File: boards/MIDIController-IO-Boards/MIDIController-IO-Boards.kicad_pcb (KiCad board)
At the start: 2 copper layers, 150 x 100 mm, 51 parts, among them J1 KeyboardCtrl, J10 I2C, J11 LTC4311_1, J12 IO_Boards, J13 I2C2, J14 DC12V, J15 LTC4311_2, J2 TechnicsCtrl, J3 StopLeftCtrl, J4 StopRightCtrl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

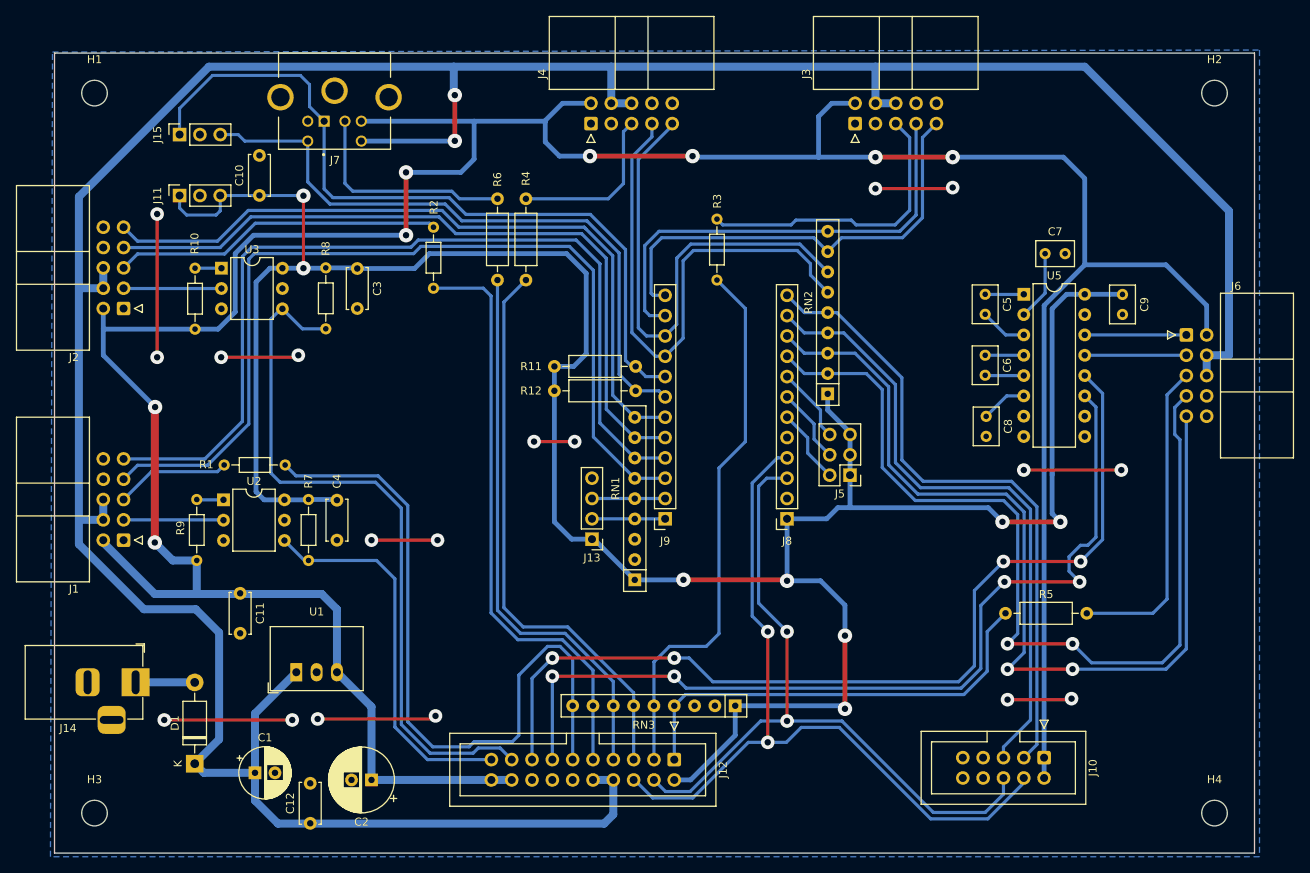
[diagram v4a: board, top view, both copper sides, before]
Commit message: Updated design rules to 0.32mm template and exported Gerber files
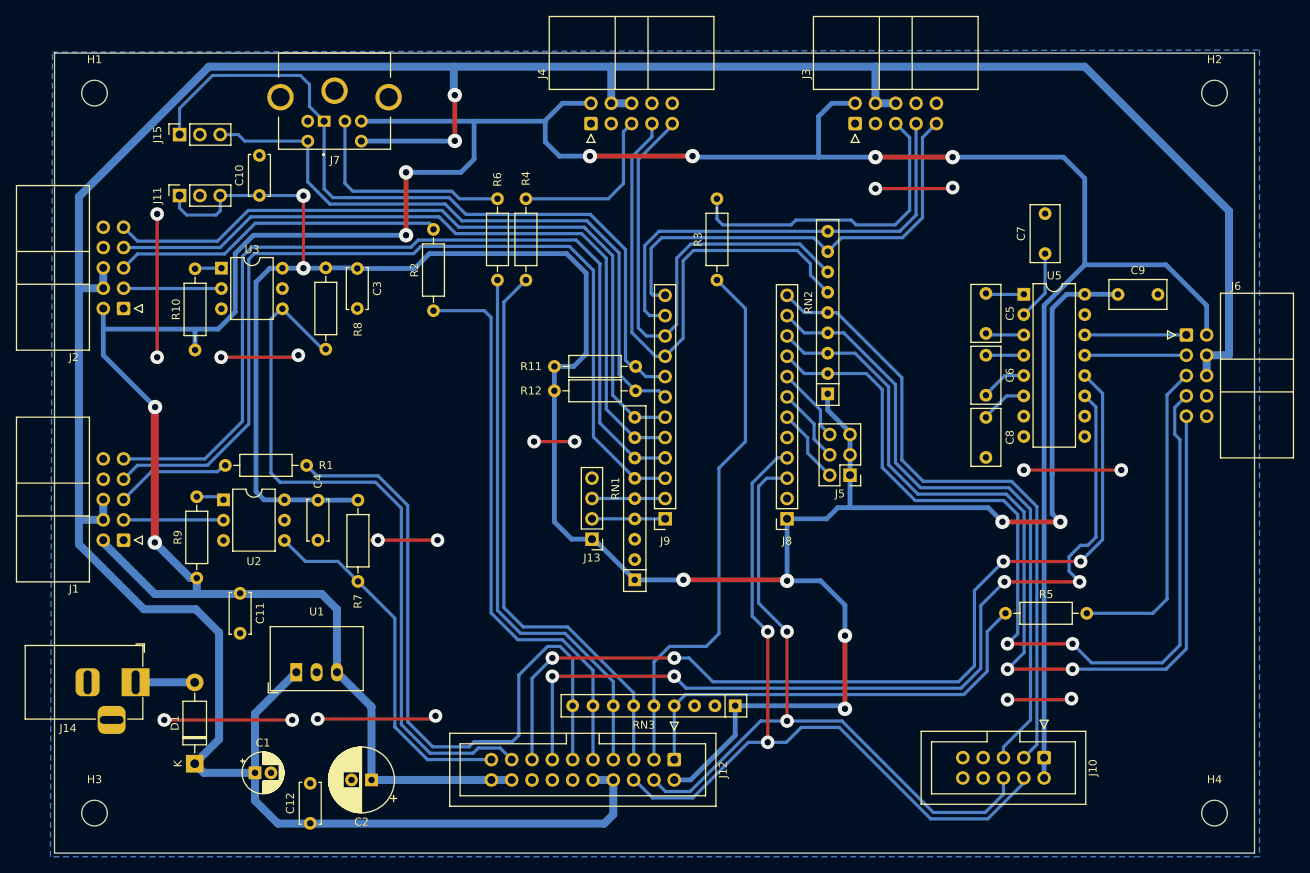
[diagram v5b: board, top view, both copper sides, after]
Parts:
- C1: footprint Capacitor_THT:CP_Radial_D6.3mm_P2.50mm -> Capacitor_THT:CP_Radial_D5.0mm_P2.00mm
- C5, C6, C7, C8, C9: footprint Capacitor_THT:C_Rect_L4.6mm_W3.0mm_P2.50mm_MKS02_FKP02 -> Capacitor_THT:C_Rect_L7.0mm_W3.5mm_P5.00mm
- R1, R10, R2, R3, R7, R8, R9: footprint Resistor_THT:R_Axial_DIN0204_L3.6mm_D1.6mm_P7.62mm_Horizontal -> Resistor_THT:R_Axial_DIN0207_L6.3mm_D2.5mm_P10.16mm_Horizontal
- moved R7 6.18 mm to (106.0, 96.3)
- moved R2 2.81 mm to (115.4, 72.7)
- moved R1 2.68 mm to (99.6, 92.0)
- moved R10 2.61 mm to (85.6, 77.6)
- moved C4 2.38 mm to (101.0, 96.3)
- moved R9 2.19 mm to (85.9, 106.1)
- moved C9 0.57 mm to (201.0, 70.6), turned to 0 degrees
- moved C5 0.15 mm to (184.5, 70.5)
- moved C8 0.13 mm to (184.5, 86.0)
- moved C6 0.10 mm to (184.5, 78.2)
- turned C7 to 90 degrees
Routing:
- net /RXD_Kbd: track 48.1 -> 45.2 mm
- net +3.3V: track 318.8 -> 321.6 mm
- net /IntTechnics: track 74.1 -> 71.4 mm
- net /IntKeyboard: track 89.2 -> 86.5 mm
- net Net-(J3-Pin_5): track 37.2 -> 39.7 mm
- net +5V: track 394.4 -> 395.8 mm
- net Net-(U5-C2-): track 4.70 -> 5.84 mm
- net /RXD_Technics: track 88.8 -> 89.9 mm
- net Net-(U5-C1-): track 5.89 -> 4.91 mm

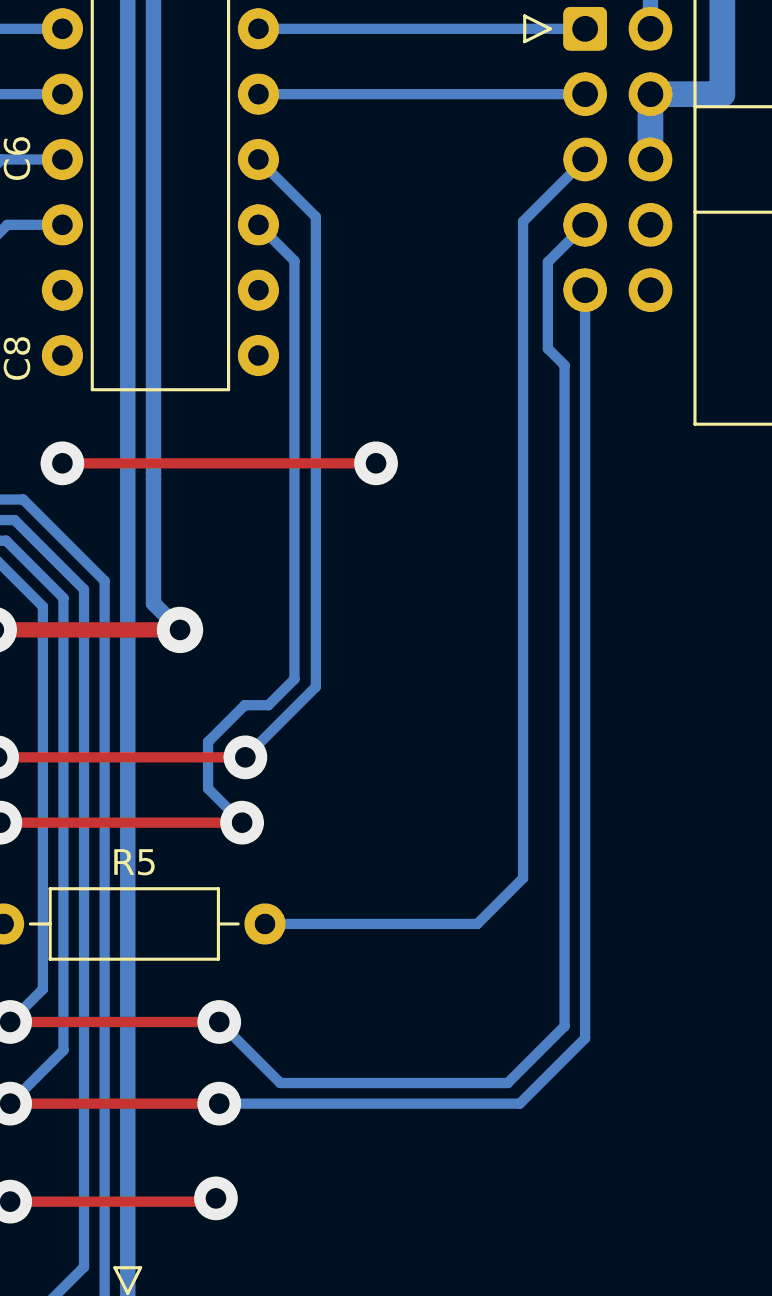
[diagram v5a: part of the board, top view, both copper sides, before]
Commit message: Fixed some RX/TX pin swaps
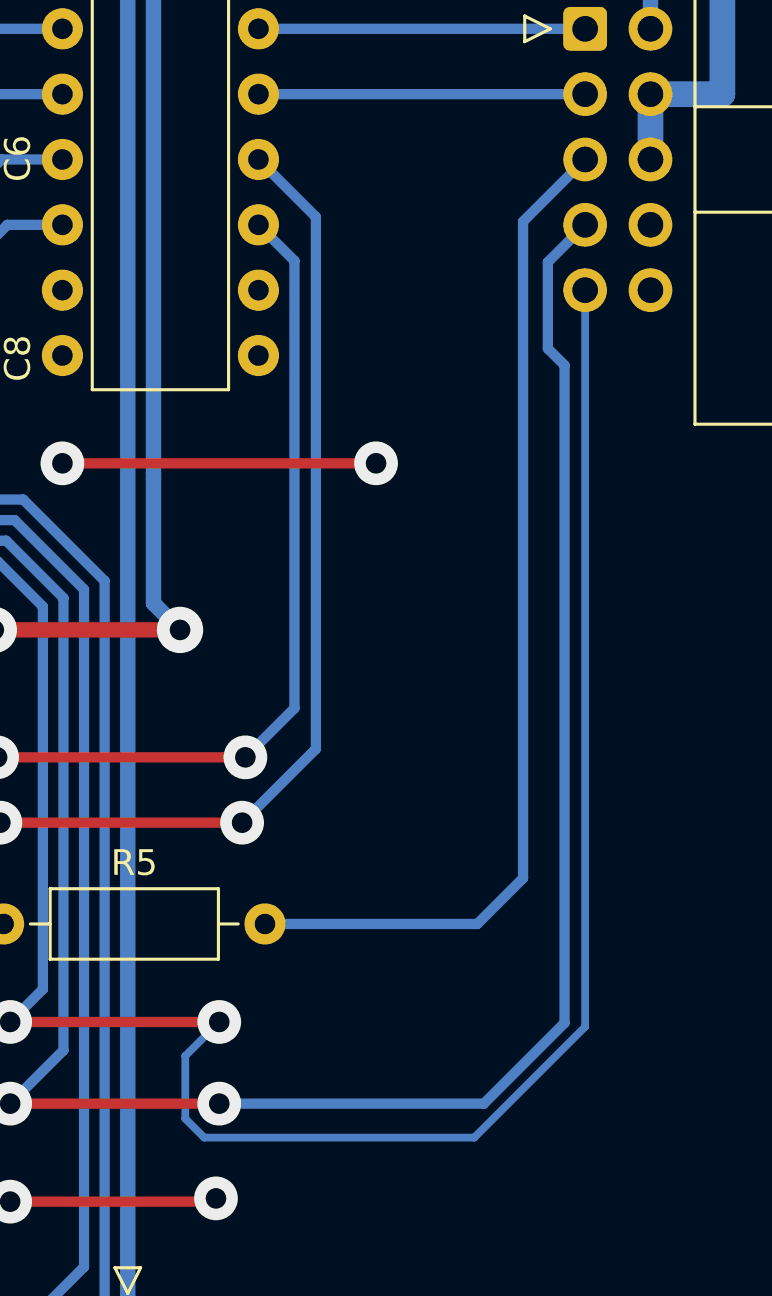
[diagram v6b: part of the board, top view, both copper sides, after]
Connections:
- J12 pad 13: /TXD_Panel -> /RXD_Panel
- J12 pad 15: /RXD_Panel -> /TXD_Panel
- J8 pad 10: /SDA_Panel -> /SCL_Panel
- J8 pad 9: /SCL_Panel -> /SDA_Panel
- RN2 pad 2: /SCL_Panel -> /SDA_Panel
- RN2 pad 3: /SDA_Panel -> /SCL_Panel
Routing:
- net /SCL_Panel: track 114.9 -> 119.7 mm
- net /RXD_Panel: track 117.8 -> 115.0 mm
- net /TXD_Panel: track 113.4 -> 114.6 mm
- net /SDA_Panel: track 117.5 -> 118.1 mm

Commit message: Fixed size of I2C expander board footprint
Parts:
- RN1, RN2: value 1.5k -> 1k
- RN3: value 1.5k -> 4k7
- moved J5 2.92 mm to (170.4, 93.2)
- moved J8 2.92 mm to (162.6, 98.7)
- moved RN2 2.92 mm to (167.6, 83.1)
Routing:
- net +3.3V: track 321.6 -> 318.1 mm
- net /SCL_StopRight: track 67.0 -> 69.9 mm
- net /SCL: track 98.7 -> 101.6 mm
- net /SDA_StopRight: track 62.2 -> 65.1 mm
- net /SDA_Panel: track 118.1 -> 115.2 mm
- net /SDA_I2C1: track 78.6 -> 75.7 mm
- net /SDA: track 90.4 -> 93.4 mm
- net /SCL_Panel: track 119.7 -> 116.8 mm
- net /SCL_I2C1: track 80.3 -> 77.3 mm
- net Net-(R9-Pad2): track 3.50 -> 2.96 mm

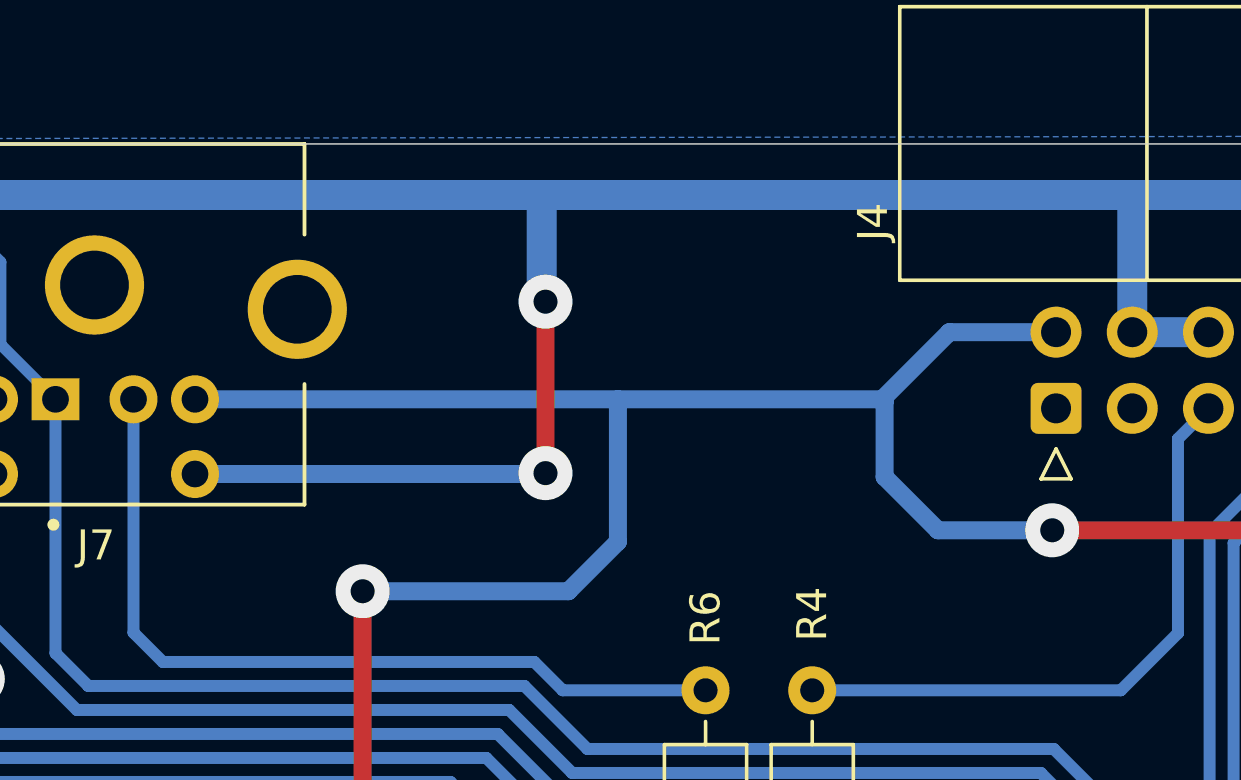
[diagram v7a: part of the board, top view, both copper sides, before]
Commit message: Make Toestud PS2 connectors symmetrical to avoid connection errors
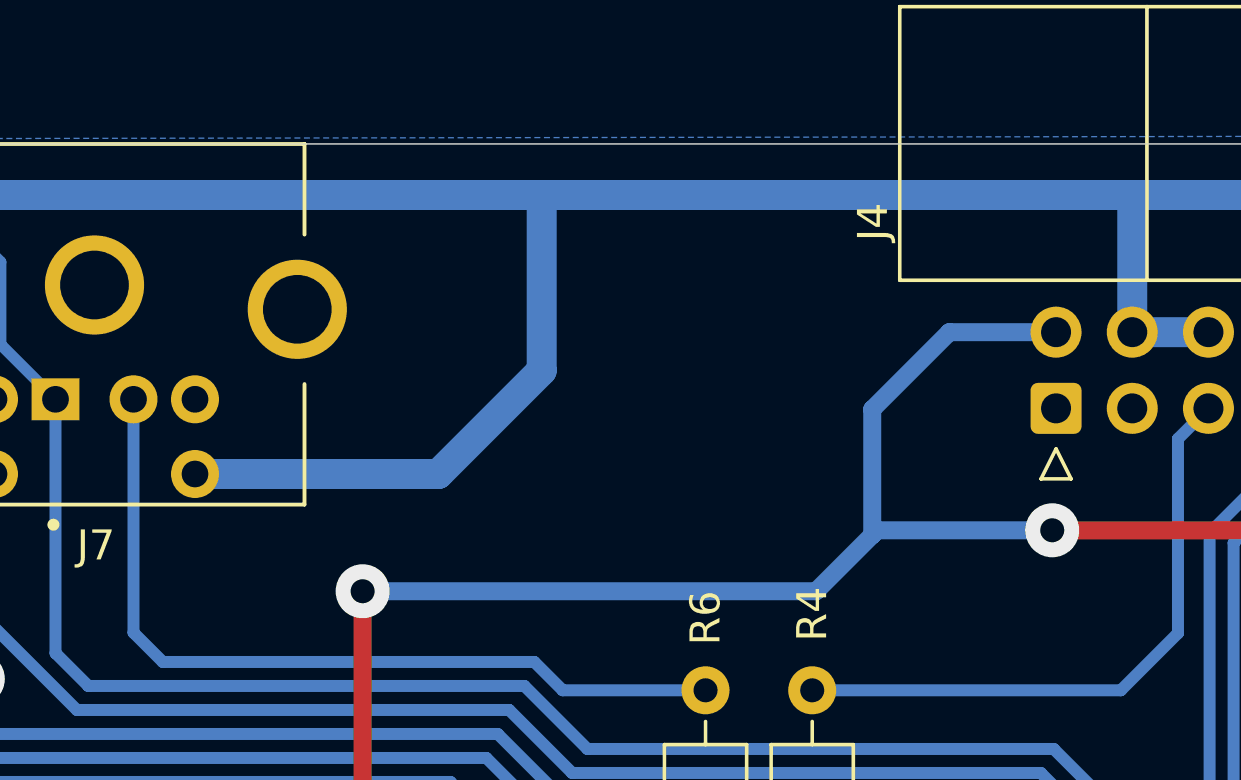
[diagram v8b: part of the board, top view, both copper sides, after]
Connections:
- J7 pad 4: +5V -> unconnected-(J7-Pad4)
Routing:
- net +5V: track 395.8 -> 378.5 mm
- net +12V: track 390.4 -> 388.3 mm, vias 2 -> 0
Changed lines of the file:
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@@
 	(net 69 "unconnected-(RN3-R2-Pad3)")
 	(net 70 "unconnected-(RN3-R1-Pad2)")
+	(net 71 "unconnected-(J7-Pad4)")
 	(footprint "Connector_IDC:IDC-Header_2x05_P2.54mm_Horizontal"
 		(layer "F.Cu")
@@
 			(layers "*.Cu" "*.Mask")
 			(remove_unused_layers no)
-			(net 4 "+5V")
-			(pintype "passive")
+			(net 71 "unconnected-(J7-Pad4)")
+			(pintype "passive+no_connect")
 			(solder_mask_margin 0.102)
 		)
@@
 	)
 	(segment
+		(start 131.572 46.736)
+		(end 135.128 46.736)
+		(width 0.6)
+		(layer "B.Cu")
+		(net 4)
+	)
+	(segment
 		(start 191.77 128.5335)
 		(end 191.77 131.0735)
@@
 	)
 	(segment
-		(start 135.001 53.34)
-		(end 131.191 53.34)
+		(start 127.128 55.372)
+		(end 129 53.5)
 		(width 0.6)
 		(layer "B.Cu")
@@
 	)
 	(segment
-		(start 129.413 49.053)
-		(end 129.334 48.974)
-		(width 0.6)
-		(layer "B.Cu")
-		(net 4)
-	)
-	(segment
 		(start 168.148 46.736)
 		(end 165.227 46.736)
@@
 	)
 	(segment
+		(start 129 49.308)
+		(end 131.572 46.736)
+		(width 0.6)
+		(layer "B.Cu")
+		(net 4)
+	)
+	(segment
 		(start 163.576 53.467)
 		(end 147.955 53.467)
@@
 	)
 	(segment
-		(start 120.523 53.721)
-		(end 120.523 48.974)
-		(width 0.6)
-		(layer "B.Cu")
-		(net 4)
-	)
-	(segment
 		(start 74.168 78.232)
 		(end 74.168 74.93)
@@
 	)
 	(segment
-		(start 112.014 55.372)
-		(end 118.872 55.372)
-		(width 0.6)
-		(layer "B.Cu")
-		(net 4)
-	)
-	(segment
-		(start 131.572 46.736)
-		(end 135.128 46.736)
+		(start 129.16 53.34)
+		(end 129 53.5)
 		(width 0.6)
 		(layer "B.Cu")
@@
 	)
 	(segment
-		(start 129.334 48.974)
-		(end 131.572 46.736)
-		(width 0.6)
-		(layer "B.Cu")
-		(net 4)
-	)
-	(segment
-		(start 118.872 55.372)
-		(end 120.523 53.721)
+		(start 112.014 55.372)
+		(end 127.128 55.372)
 		(width 0.6)
 		(layer "B.Cu")
@@
 	)
 	(segment
-		(start 106.426 48.974)
-		(end 120.523 48.974)
+		(start 129 53.5)
+		(end 129 49.308)
 		(width 0.6)
 		(layer "B.Cu")
@@
 	)
 	(segment
+		(start 135.001 53.34)
+		(end 129.16 53.34)
+		(width 0.6)
+		(layer "B.Cu")
+		(net 4)
+	)
+	(segment
 		(start 103.378 117.856)
 		(end 103.378 109.982)
@@
 	)
 	(segment
-		(start 120.523 48.974)
-		(end 129.334 48.974)
-		(width 0.6)
-		(layer "B.Cu")
-		(net 4)
-	)
-	(segment
 		(start 90.659711 65.513711)
 		(end 92.943422 63.23)
@@
 	)
 	(segment
-		(start 131.191 53.34)
-		(end 129.413 51.562)
-		(width 0.6)
-		(layer "B.Cu")
-		(net 4)
-	)
-	(segment
 		(start 107.578651 122.056651)
 		(end 103.378 117.856)
@@
 	)
 	(segment
-		(start 129.413 51.562)
-		(end 129.413 49.053)
-		(width 0.6)
-		(layer "B.Cu")
-		(net 4)
-	)
-	(segment
-		(start 118.11 51.435)
-		(end 118.11 45.72)
-		(width 0.6)
-		(layer "F.Cu")
-		(net 5)
-	)
-	(via
-		(at 118.11 45.72)
-		(size 1.8)
-		(drill 0.8)
-		(layers "F.Cu" "B.Cu")
-		(net 5)
-	)
-	(via
-		(at 118.11 51.435)
-		(size 1.8)
-		(drill 0.8)
-		(layers "F.Cu" "B.Cu")
-		(net 5)
-	)
-	(segment
 		(start 88.646 126.238)
 		(end 85.598 129.286)
@@
 	)
 	(segment
-		(start 71.12 98.806)
-		(end 71.12 69.85)
+		(start 114.536 51.464)
+		(end 106.426 51.464)
 		(width 1)
 		(layer "B.Cu")
@@
 	)
 	(segment
-		(start 71.12 101.854)
-		(end 79.248 109.982)
+		(start 71.12 98.806)
+		(end 71.12 69.85)
 		(width 1)
 		(layer "B.Cu")
@@
 	)
 	(segment
-		(start 117.983 42.164)
-		(end 117.983 45.593)
+		(start 71.12 101.854)
+		(end 79.248 109.982)
 		(width 1)
 		(layer "B.Cu")
@@
 	)
 	(segment
+		(start 117.983 48.017)
+		(end 114.536 51.464)
+		(width 1)
+		(layer "B.Cu")
+		(net 5)
+	)
+	(segment
 		(start 74.168 98.806)
 		(end 74.168 96.266)
@@
 	)
 	(segment
-		(start 117.983 45.593)
-		(end 118.11 45.72)
-		(width 1)
-		(layer "B.Cu")
-		(net 5)
-	)
-	(segment
-		(start 106.426 51.464)
-		(end 118.081 51.464)
-		(width 0.6)
-		(layer "B.Cu")
-		(net 5)
-	)
-	(segment
 		(start 79.248 109.982)
 		(end 85.725 109.982)
@@
 	)
 	(segment
-		(start 118.081 51.464)
-		(end 118.11 51.435)
-		(width 0.6)
-		(layer "B.Cu")
-		(net 5)
-	)
-	(segment
 		(start 170.688 42.164)
 		(end 196.85 42.164)
@@
 		(width 1)
 		(layer "B.Cu")
+		(net 5)
+	)
+	(segment
+		(start 117.983 42.164)
+		(end 117.983 48.017)
+		(width 1)
+		(layer "B.Cu")
